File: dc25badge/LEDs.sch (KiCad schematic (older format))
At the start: 60 parts, among them U10 APA102, U11 APA102, U12 APA102, U13 APA102, U14 APA102, U15 APA102, U16 APA102, U17 APA102, U18 APA102, U19 APA102, U20 APA102, U21 APA102, U22 APA102, U23 APA102, U24 APA102, U25 APA102, U26 APA102, U27 APA102, U28 APA102, U29 APA102, U30 APA102, U31 APA102, U32 APA102, U33 APA102, U34 APA102, U35 APA102, U36 APA102, U37 APA102, U38 APA102, U39 APA102, U40 APA102, U41 APA102, U42 APA102, U43 APA102, U44 APA102, U45 APA102, U46 APA102, U47 APA102, U48 APA102, U49 APA102, U5 APA102, U50 APA102, U51 APA102, U52 APA102, U53 APA102, U54 APA102, U55 APA102, U56 APA102, U57 APA102, U58 APA102, U59 APA102, U6 APA102, U60 APA102, U61 APA102, U62 APA102, U63 APA102, U64 APA102, U7 APA102, U8 APA102, U9 APA102

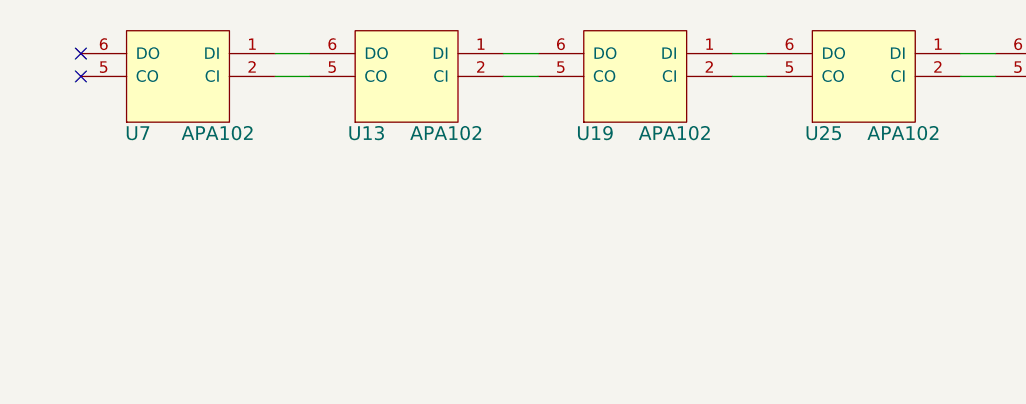
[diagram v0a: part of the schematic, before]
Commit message: First letter routed.
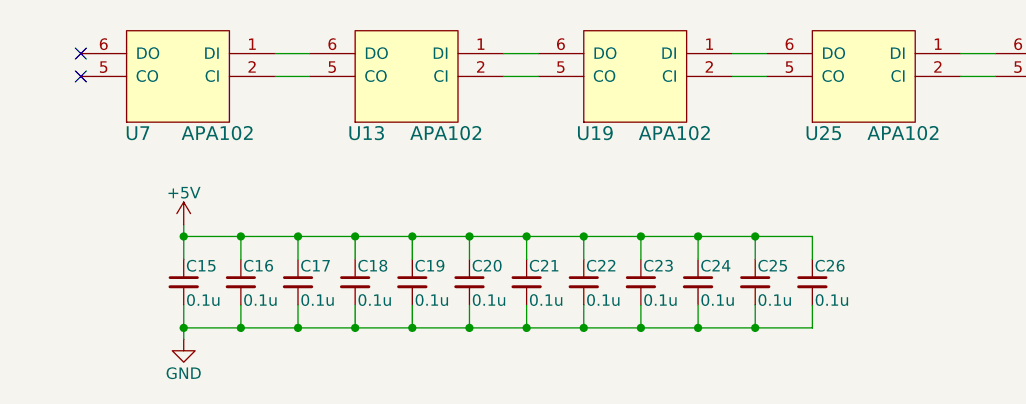
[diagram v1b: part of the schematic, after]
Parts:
- added C15, C16, C17, C18, C19, C20, C21, C22, C23, C24, C25, C26: 0.1u, Capacitors_SMD:C_0805_HandSoldering, symbol C_Small
- U10, U11, U12, U13, U14, U15, U16, U17, U18, U19, U20, U21, U22, U23, U24, U25, U26, U27, U28, U29, U30, U31, U32, U33, U34, U35, U36, U37, U38, U39, U40, U41, U42, U43, U44, U45, U46, U47, U48, U49, U5, U50, U51, U52, U53, U54, U55, U56, U57, U58, U59, U6, U60, U61, U62, U63, U64, U7, U8, U9: footprint (none) -> Badge_Parts:APA102
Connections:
- net +5V: now also C15.1, C16.1, C17.1, C18.1, C19.1, C20.1, C21.1, C22.1, C23.1, C24.1, C25.1, C26.1
- net GND: now also C15.2, C16.2, C17.2, C18.2, C19.2, C20.2, C21.2, C22.2, C23.2, C24.2, C25.2, C26.2

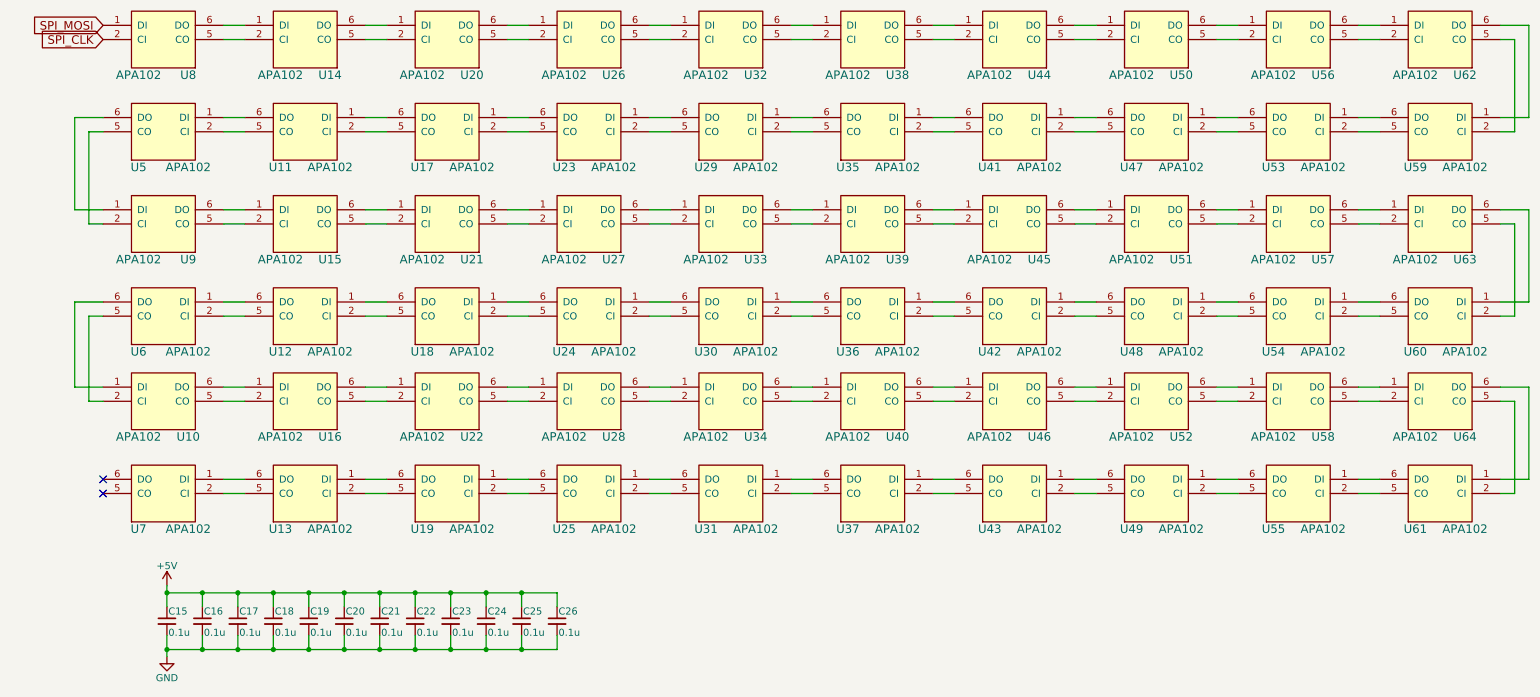
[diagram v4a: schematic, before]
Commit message: Schematic changes for 48 LED version.
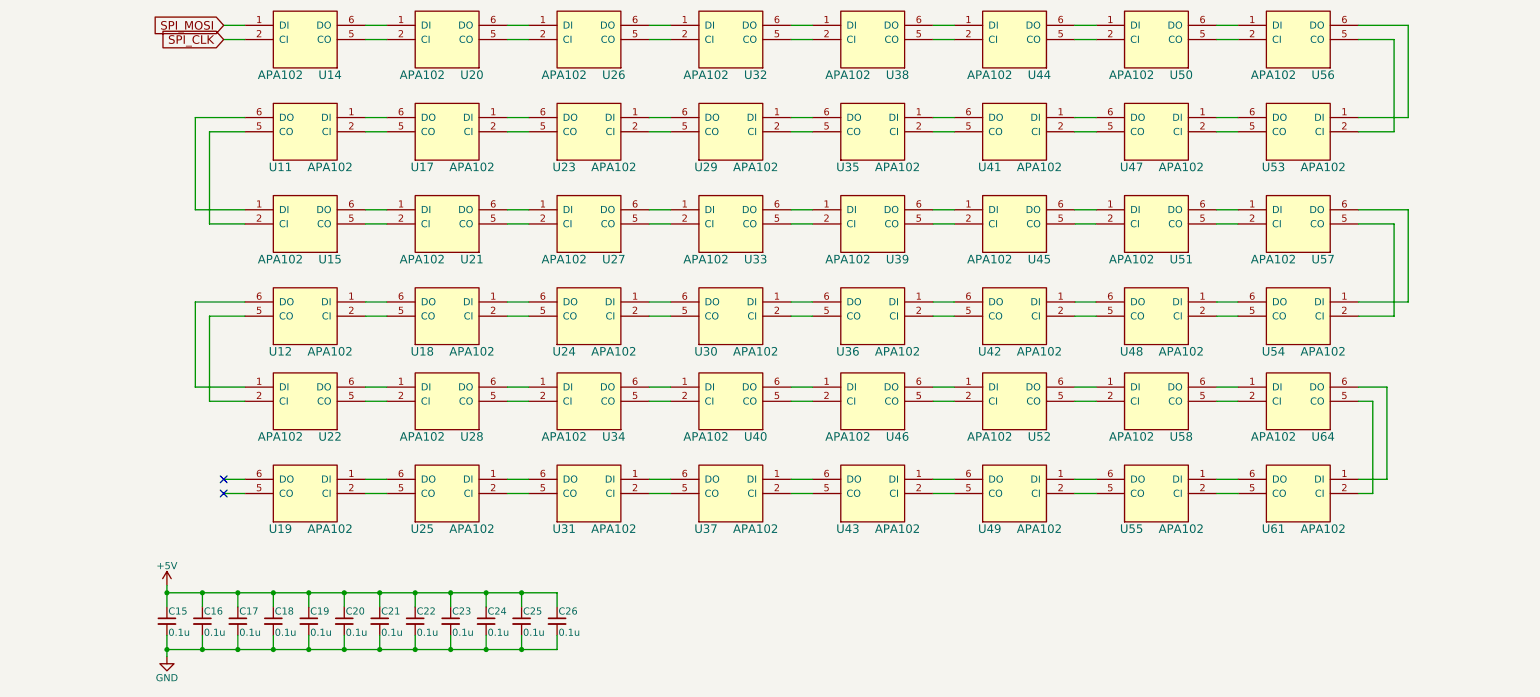
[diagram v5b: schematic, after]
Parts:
- removed U10, U13, U16, U5, U59, U6, U60, U62, U63, U7, U8, U9: APA102, Badge_Parts:APA102, symbol APA102
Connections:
- net SPI_CLK: now also U14.2 (CI)
- net SPI_MOSI: now also U14.1 (DI)
- net at U56.5 (CO): now also U53.2 (CI)
- net at U56.6 (DO): now also U53.1 (DI)
- net at U11.5 (CO): now also U15.2 (CI)
- net at U11.6 (DO): now also U15.1 (DI)
- net at U57.5 (CO): now also U54.2 (CI)
- net at U57.6 (DO): now also U54.1 (DI)
- net at U12.5 (CO): now also U22.2 (CI)
- net at U12.6 (DO): now also U22.1 (DI)
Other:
- moved on the sheet: U19, U22, U25, U28, U31, U34, U37, U40, U43, U46, U49, U52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

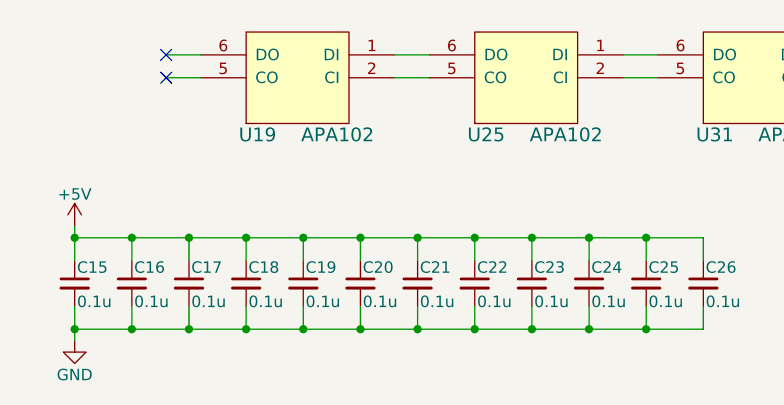
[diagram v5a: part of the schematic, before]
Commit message: 48 LED rebuild.
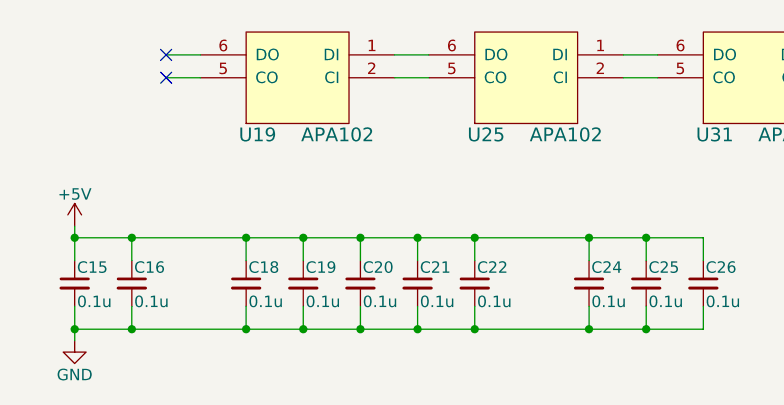
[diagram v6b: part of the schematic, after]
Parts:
- removed C17, C23: 0.1u, Capacitors_SMD:C_0805_HandSoldering, symbol C_Small
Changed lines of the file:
@@
-$EndComp
-$Comp
-L C_Small C17
-U 1 1 592BE090
-P 1900 5150
-F 0 "C17" H 1910 5220 50  0000 L CNN
-F 1 "0.1u" H 1910 5070 50  0000 L CNN
-F 2 "Capacitors_SMD:C_0805_HandSoldering" H 1900 5150 50  0001 C CNN
-F 3 "" H 1900 5150 50  0000 C CNN
-	1    1900 5150
-	1    0    0    -1
 $EndComp
 $Comp
@@
 $EndComp
 $Comp
-L C_Small C23
-U 1 1 592BE478
-P 3400 5150
-F 0 "C23" H 3410 5220 50  0000 L CNN
-F 1 "0.1u" H 3410 5070 50  0000 L CNN
-F 2 "Capacitors_SMD:C_0805_HandSoldering" H 3400 5150 50  0001 C CNN
-F 3 "" H 3400 5150 50  0000 C CNN
-	1    3400 5150
-	1    0    0    -1
-$EndComp
-$Comp
 L C_Small C24
 U 1 1 592BE47E
@@
 Connection ~ 1400 4950
 Connection ~ 1650 4950
-Connection ~ 1900 4950
 Connection ~ 2150 4950
 Connection ~ 2400 4950
@@
 Connection ~ 3650 5350
 Wire Wire Line
-	3400 5250 3400 5350
-Connection ~ 3400 5350
-Wire Wire Line
 	3150 5250 3150 5350
 Connection ~ 3150 5350
@@
 	2150 5250 2150 5350
 Connection ~ 2150 5350
-Wire Wire Line
-	1900 5250 1900 5350
-Connection ~ 1900 5350
 Wire Wire Line
 	1650 5250 1650 5350
@@
 Connection ~ 3650 4950
 Wire Wire Line
-	3400 5050 3400 4950
-Connection ~ 3400 4950
-Wire Wire Line
 	3150 5050 3150 4950
 Connection ~ 3150 4950
@@
 	2150 5050 2150 4950
 Wire Wire Line
-	1900 5050 1900 4950
-Wire Wire Line
 	1650 5050 1650 4950

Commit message: Add reverse polarity MOSFET.
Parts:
- C15, C16, C18, C19, C20, C21, C22, C24, C25, C26: footprint Capacitors_SMD:C_0805_HandSoldering -> Capacitors_SMD:C_0805
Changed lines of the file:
@@
 F 0 "C15" H 1410 5220 50  0000 L CNN
 F 1 "0.1u" H 1410 5070 50  0000 L CNN
-F 2 "Capacitors_SMD:C_0805_HandSoldering" H 1400 5150 50  0001 C CNN
+F 2 "Capacitors_SMD:C_0805" H 1400 5150 50  0001 C CNN
 F 3 "" H 1400 5150 50  0000 C CNN
 	1    1400 5150
@@
 F 0 "C16" H 1660 5220 50  0000 L CNN
 F 1 "0.1u" H 1660 5070 50  0000 L CNN
-F 2 "Capacitors_SMD:C_0805_HandSoldering" H 1650 5150 50  0001 C CNN
+F 2 "Capacitors_SMD:C_0805" H 1650 5150 50  0001 C CNN
 F 3 "" H 1650 5150 50  0000 C CNN
 	1    1650 5150
@@
 F 0 "C18" H 2160 5220 50  0000 L CNN
 F 1 "0.1u" H 2160 5070 50  0000 L CNN
-F 2 "Capacitors_SMD:C_0805_HandSoldering" H 2150 5150 50  0001 C CNN
+F 2 "Capacitors_SMD:C_0805" H 2150 5150 50  0001 C CNN
 F 3 "" H 2150 5150 50  0000 C CNN
 	1    2150 5150
@@
 F 0 "C19" H 2410 5220 50  0000 L CNN
 F 1 "0.1u" H 2410 5070 50  0000 L CNN
-F 2 "Capacitors_SMD:C_0805_HandSoldering" H 2400 5150 50  0001 C CNN
+F 2 "Capacitors_SMD:C_0805" H 2400 5150 50  0001 C CNN
 F 3 "" H 2400 5150 50  0000 C CNN
 	1    2400 5150
@@
 F 0 "C20" H 2660 5220 50  0000 L CNN
 F 1 "0.1u" H 2660 5070 50  0000 L CNN
-F 2 "Capacitors_SMD:C_0805_HandSoldering" H 2650 5150 50  0001 C CNN
+F 2 "Capacitors_SMD:C_0805" H 2650 5150 50  0001 C CNN
 F 3 "" H 2650 5150 50  0000 C CNN
 	1    2650 5150
@@
 F 0 "C21" H 2910 5220 50  0000 L CNN
 F 1 "0.1u" H 2910 5070 50  0000 L CNN
-F 2 "Capacitors_SMD:C_0805_HandSoldering" H 2900 5150 50  0001 C CNN
+F 2 "Capacitors_SMD:C_0805" H 2900 5150 50  0001 C CNN
 F 3 "" H 2900 5150 50  0000 C CNN
 	1    2900 5150
@@
 F 0 "C22" H 3160 5220 50  0000 L CNN
 F 1 "0.1u" H 3160 5070 50  0000 L CNN
-F 2 "Capacitors_SMD:C_0805_HandSoldering" H 3150 5150 50  0001 C CNN
+F 2 "Capacitors_SMD:C_0805" H 3150 5150 50  0001 C CNN
 F 3 "" H 3150 5150 50  0000 C CNN
 	1    3150 5150
@@
 F 0 "C24" H 3660 5220 50  0000 L CNN
 F 1 "0.1u" H 3660 5070 50  0000 L CNN
-F 2 "Capacitors_SMD:C_0805_HandSoldering" H 3650 5150 50  0001 C CNN
+F 2 "Capacitors_SMD:C_0805" H 3650 5150 50  0001 C CNN
 F 3 "" H 3650 5150 50  0000 C CNN
 	1    3650 5150
@@
 F 0 "C25" H 3910 5220 50  0000 L CNN
 F 1 "0.1u" H 3910 5070 50  0000 L CNN
-F 2 "Capacitors_SMD:C_0805_HandSoldering" H 3900 5150 50  0001 C CNN
+F 2 "Capacitors_SMD:C_0805" H 3900 5150 50  0001 C CNN
 F 3 "" H 3900 5150 50  0000 C CNN
 	1    3900 5150
@@
 F 0 "C26" H 4160 5220 50  0000 L CNN
 F 1 "0.1u" H 4160 5070 50  0000 L CNN
-F 2 "Capacitors_SMD:C_0805_HandSoldering" H 4150 5150 50  0001 C CNN
+F 2 "Capacitors_SMD:C_0805" H 4150 5150 50  0001 C CNN
 F 3 "" H 4150 5150 50  0000 C CNN
 	1    4150 5150
@@
 $EndComp
 $Comp
-L +5V #PWR027
+L +5V #PWR028
 U 1 1 592BE4DA
 P 1400 4900
-F 0 "#PWR027" H 1400 4750 50  0001 C CNN
+F 0 "#PWR028" H 1400 4750 50  0001 C CNN
 F 1 "+5V" H 1400 5040 50  0000 C CNN
 F 2 "" H 1400 4900 50  0000 C CNN
@@
 	1700 3600 1700 3000
 $Comp
-L GND #PWR028
+L GND #PWR029
 U 1 1 592BE989
 P 1400 5400
-F 0 "#PWR028" H 1400 5150 50  0001 C CNN
+F 0 "#PWR029" H 1400 5150 50  0001 C CNN
 F 1 "GND" H 1400 5250 50  0000 C CNN
 F 2 "" H 1400 5400 50  0000 C CNN
